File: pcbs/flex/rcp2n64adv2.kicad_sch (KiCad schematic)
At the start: 17 parts, among them J1 Conn_01x01, J2 Conn_01x01, J3 Conn_01x01, J3.1 Conn_01x01, J4 Conn_01x01, J5 Conn_01x01, J6 Conn_01x30, U1 74LVC1G17, X1 n64_rcp_vid_aud_out_no_3v3_con, X2 Conn_01x01

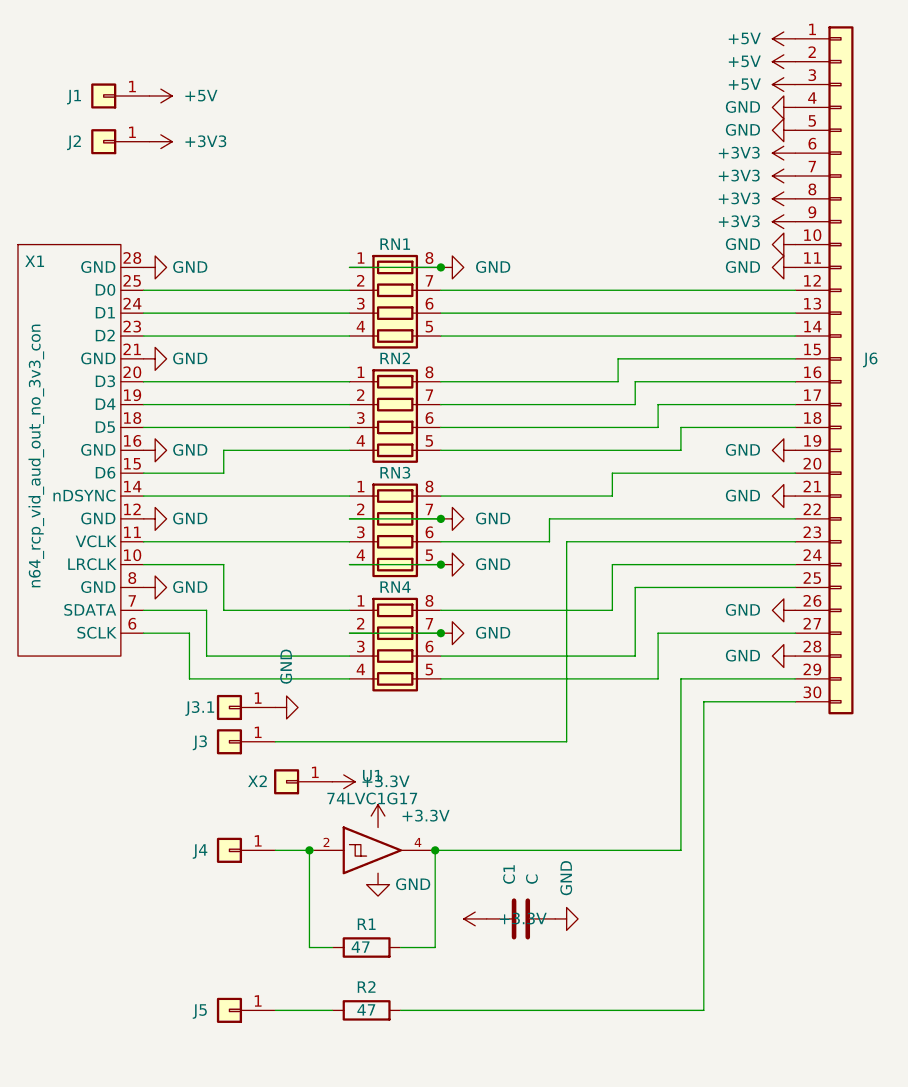
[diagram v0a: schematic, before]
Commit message: update flex PCB with minor changes, e.g. added a logo
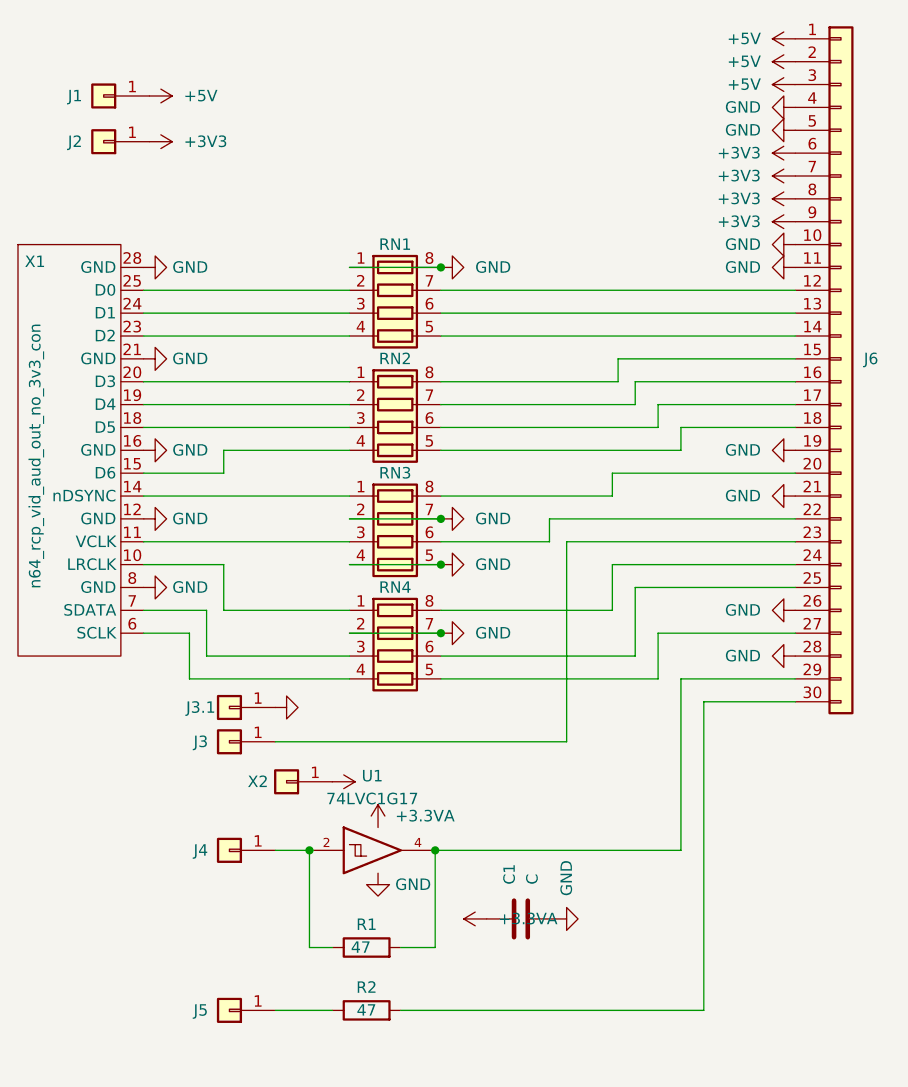
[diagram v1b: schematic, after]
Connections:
- net +3V3: no longer C1.1, U1.5 (VCC), X2.1 (Pin_1)
- new net +3.3VA: C1.1, U1.5 (VCC), X2.1 (Pin_1)
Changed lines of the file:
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@@
       (effects (font (size 1.27 1.27)) hide)
     )
-    (property "Value" "GND" (id 1) (at 74.9299 126.365 0)
+    (property "Value" "" (id 1) (at 74.9299 126.365 0)
       (effects (font (size 1.27 1.27)) (justify left))
     )
@@
     (pin "1")
   )
+  (symbol (lib_id "power:+3.3VA") (at 97.155 152.4 90) (unit 1)
+    (in_bom yes) (on_board yes) (fields_autoplaced)
+    (property "Reference" "#PWR?" (id 0) (at 100.965 152.4 0)
+      (effects (font (size 1.27 1.27)) hide)
+    )
+    (property "Value" "+3.3VA" (id 1) (at 98.425 152.3999 90)
+      (effects (font (size 1.27 1.27)) (justify right))
+    )
+    (property "Footprint" "" (id 2) (at 97.155 152.4 0)
+      (effects (font (size 1.27 1.27)) hide)
+    )
+    (property "Datasheet" "" (id 3) (at 97.155 152.4 0)
+      (effects (font (size 1.27 1.27)) hide)
+    )
+    (pin "1")
+  )
   (symbol (lib_id "Connector_Generic:Conn_01x01") (at 68.58 162.56 180) (unit 1)
     (in_bom no) (on_board yes)
@@
     )
     (property "Datasheet" "" (id 3) (at 59.055 115.57 0)
+      (effects (font (size 1.27 1.27)) hide)
+    )
+    (pin "1")
+  )
+  (symbol (lib_id "power:+3.3VA") (at 80.01 137.16 270) (unit 1)
+    (in_bom yes) (on_board yes) (fields_autoplaced)
+    (property "Reference" "#PWR?" (id 0) (at 76.2 137.16 0)
+      (effects (font (size 1.27 1.27)) hide)
+    )
+    (property "Value" "" (id 1) (at 83.82 137.1599 90)
+      (effects (font (size 1.27 1.27)) (justify left))
+    )
+    (property "Footprint" "" (id 2) (at 80.01 137.16 0)
+      (effects (font (size 1.27 1.27)) hide)
+    )
+    (property "Datasheet" "" (id 3) (at 80.01 137.16 0)
       (effects (font (size 1.27 1.27)) hide)
     )
@@
     (pin "1")
   )
-  (symbol (lib_id "power:+3.3V") (at 85.09 142.24 0) (unit 1)
-    (in_bom yes) (on_board yes) (fields_autoplaced)
-    (property "Reference" "#PWR0131" (id 0) (at 85.09 146.05 0)
-      (effects (font (size 1.27 1.27)) hide)
-    )
-    (property "Value" "+3.3V" (id 1) (at 87.63 140.9699 0)
-      (effects (font (size 1.27 1.27)) (justify left))
-    )
-    (property "Footprint" "" (id 2) (at 85.09 142.24 0)
-      (effects (font (size 1.27 1.27)) hide)
-    )
-    (property "Datasheet" "" (id 3) (at 85.09 142.24 0)
-      (effects (font (size 1.27 1.27)) hide)
-    )
-    (pin "1")
-  )
   (symbol (lib_id "power:GND") (at 92.075 120.65 90) (unit 1)
     (in_bom yes) (on_board yes) (fields_autoplaced)
@@
     (pin "1")
   )
-  (symbol (lib_id "power:+3.3V") (at 97.155 152.4 90) (unit 1)
-    (in_bom yes) (on_board yes) (fields_autoplaced)
-    (property "Reference" "#PWR0132" (id 0) (at 100.965 152.4 0)
-      (effects (font (size 1.27 1.27)) hide)
-    )
-    (property "Value" "+3.3V" (id 1) (at 98.425 152.3999 90)
-      (effects (font (size 1.27 1.27)) (justify right))
-    )
-    (property "Footprint" "" (id 2) (at 97.155 152.4 0)
-      (effects (font (size 1.27 1.27)) hide)
-    )
-    (property "Datasheet" "" (id 3) (at 97.155 152.4 0)
-      (effects (font (size 1.27 1.27)) hide)
-    )
-    (pin "1")
-  )
   (symbol (lib_id "power:GND") (at 92.075 113.03 90) (unit 1)
     (in_bom yes) (on_board yes) (fields_autoplaced)
@@
     (pin "1")
   )
-  (symbol (lib_id "power:+3.3V") (at 80.01 137.16 270) (unit 1)
-    (in_bom yes) (on_board yes) (fields_autoplaced)
-    (property "Reference" "#PWR0128" (id 0) (at 76.2 137.16 0)
-      (effects (font (size 1.27 1.27)) hide)
-    )
-    (property "Value" "+3.3V" (id 1) (at 83.185 137.1599 90)
-      (effects (font (size 1.27 1.27)) (justify left))
-    )
-    (property "Footprint" "" (id 2) (at 80.01 137.16 0)
-      (effects (font (size 1.27 1.27)) hide)
-    )
-    (property "Datasheet" "" (id 3) (at 80.01 137.16 0)
+  (symbol (lib_id "power:+3.3VA") (at 85.09 142.24 0) (unit 1)
+    (in_bom yes) (on_board yes) (fields_autoplaced)
+    (property "Reference" "#PWR?" (id 0) (at 85.09 146.05 0)
+      (effects (font (size 1.27 1.27)) hide)
+    )
+    (property "Value" "+3.3VA" (id 1) (at 86.995 140.9699 0)
+      (effects (font (size 1.27 1.27)) (justify left))
+    )
+    (property "Footprint" "" (id 2) (at 85.09 142.24 0)
+      (effects (font (size 1.27 1.27)) hide)
+    )
+    (property "Datasheet" "" (id 3) (at 85.09 142.24 0)
       (effects (font (size 1.27 1.27)) hide)
     )
@@
       (reference "#PWR0127") (unit 1) (value "GND") (footprint "")
     )
-    (path "/ebb00ccd-2cad-4af3-a4f4-9438755cb2c5"
-      (reference "#PWR0128") (unit 1) (value "+3.3V") (footprint "")
-    )
     (path "/b2464271-55c9-4c32-af2d-a4274a0cfecc"
       (reference "#PWR0129") (unit 1) (value "GND") (footprint "")
@@
       (reference "#PWR0130") (unit 1) (value "GND") (footprint "")
     )
-    (path "/d570e93c-5545-48d4-af35-1e19dc141390"
-      (reference "#PWR0131") (unit 1) (value "+3.3V") (footprint "")
-    )
-    (path "/e26c6331-4e64-4c88-af8e-b4f5a8b35c72"
-      (reference "#PWR0132") (unit 1) (value "+3.3V") (footprint "")
+    (path "/a2c5c77a-ce8a-4ada-ae7a-3089f5e18dfa"
+      (reference "#PWR?") (unit 1) (value "+3.3VA") (footprint "")
+    )
+    (path "/b68922d3-d7bc-4a97-8a9b-74840f074a00"
+      (reference "#PWR?") (unit 1) (value "+3.3VA") (footprint "")
+    )
+    (path "/e9ff7066-aa8f-4937-aa8c-dac2c54d75e7"
+      (reference "#PWR?") (unit 1) (value "+3.3VA") (footprint "")
     )
     (path "/fe28d019-2901-415f-bbfb-9066de361fb0"

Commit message: update main PCB with minor changes, e.g. ensure that solder mask bridges between 0.5mm pitched pads has min. 0.1mm thickness
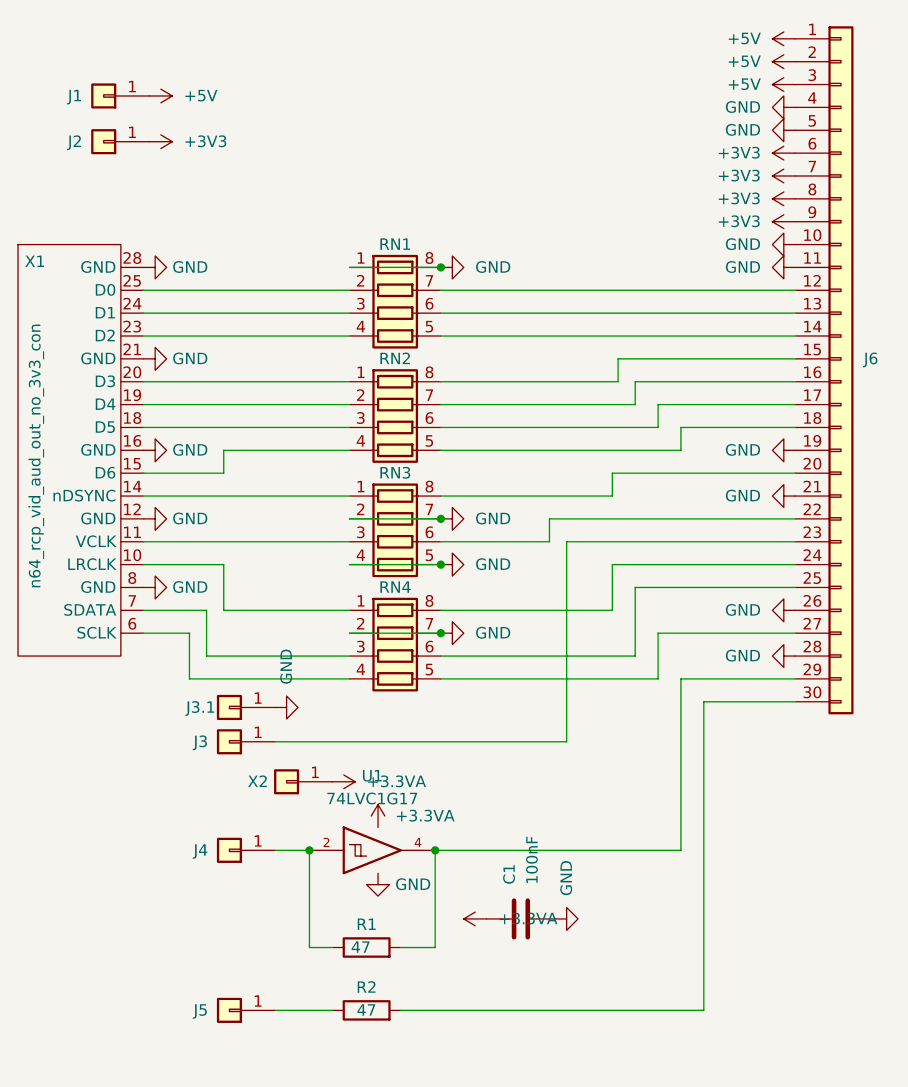
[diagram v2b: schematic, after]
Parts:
- C1: value C -> 100nF
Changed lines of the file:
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@@
       (effects (font (size 1.27 1.27)) hide)
     )
-    (property "Value" "" (id 1) (at 74.9299 126.365 0)
+    (property "Value" "GND" (id 1) (at 74.9299 126.365 0)
       (effects (font (size 1.27 1.27)) (justify left))
     )
@@
       (effects (font (size 1.27 1.27)) hide)
     )
-    (property "Value" "" (id 1) (at 83.82 137.1599 90)
+    (property "Value" "+3.3VA" (id 1) (at 83.82 137.1599 90)
       (effects (font (size 1.27 1.27)) (justify left))
     )
@@
       (effects (font (size 1.27 1.27)) (justify left))
     )
-    (property "Value" "C" (id 1) (at 102.2349 148.59 0)
+    (property "Value" "100nF" (id 1) (at 102.2349 148.59 0)
       (effects (font (size 1.27 1.27)) (justify left))
     )
@@
     )
     (path "/fe28d019-2901-415f-bbfb-9066de361fb0"
-      (reference "C1") (unit 1) (value "C") (footprint "Capacitor_SMD:C_0603_1608Metric_Pad1.08x0.95mm_HandSolder")
+      (reference "C1") (unit 1) (value "100nF") (footprint "Capacitor_SMD:C_0603_1608Metric_Pad1.08x0.95mm_HandSolder")
     )
     (path "/67679f6e-1f3a-4f43-8e31-3367e2bcf78f"

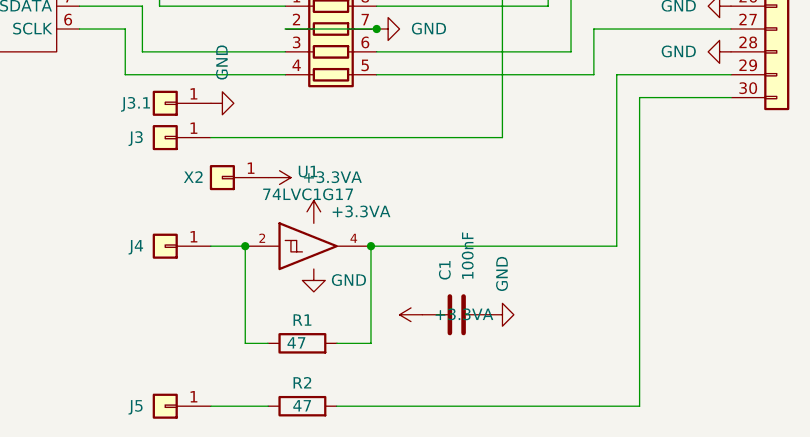
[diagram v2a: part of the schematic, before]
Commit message: update flex PCB: - add a feedback path for VI-Deblur - optimize implementation around U1 - add logo and license text to silkscreen
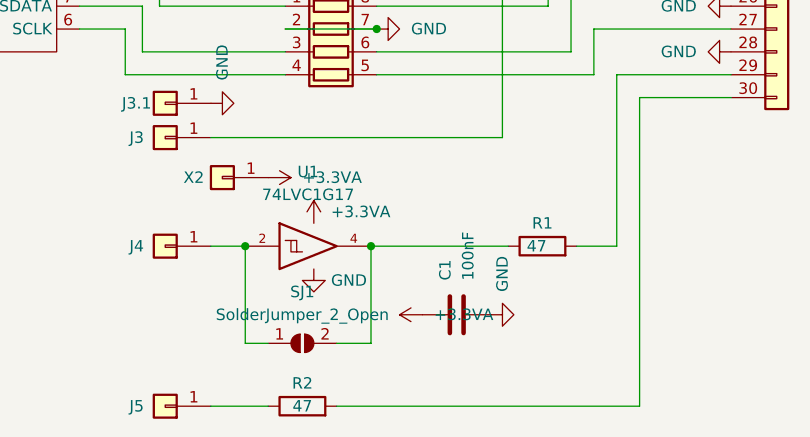
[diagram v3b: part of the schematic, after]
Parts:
- added SJ1: SolderJumper_2_Open, Jumper:SolderJumper-2_P1.3mm_Open_RoundedPad1.0x1.5mm, symbol Jumper:SolderJumper_2_Open
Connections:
- net at J4.1 (Pin_1), U1.2: now also SJ1.1 (A); no longer R1.1
- net at J6.29 (Pin_29), R1.2: no longer U1.4
- new net: R1.1, SJ1.2 (B), U1.4
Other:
- company: (none) -> Peter 'borti4938' Bartmann
- title: (none) -> RCP2N64Adv2
- moved on the sheet: R1
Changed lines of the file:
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@@
 (kicad_sch (version 20211123) (generator eeschema)
   (paper "A4")
+  (title_block
+    (title "RCP2N64Adv2")
+    (rev "v20220903")
+    (company "Peter 'borti4938' Bartmann")
+    (comment 1 "Schematic and PCB (c) 2021, 2022 by Peter Bartmann")
+    (comment 2 "Licensed under CERN-OHL-W v2")
+  )
   (junction (at 77.47 144.78) (diameter 0) (color 0 0 0 0)
   )
@@
     (stroke (width 0) (type default) (color 0 0 0 0))
   )
+  (wire (pts (xy 106.68 144.78) (xy 91.44 144.78))
+    (stroke (width 0) (type default) (color 0 0 0 0))
+  )
   (wire (pts (xy 116.205 95.25) (xy 131.445 95.25))
     (stroke (width 0) (type default) (color 0 0 0 0))
@@
     (stroke (width 0) (type default) (color 0 0 0 0))
   )
-  (wire (pts (xy 118.745 144.78) (xy 91.44 144.78))
+  (wire (pts (xy 118.745 144.78) (xy 114.3 144.78))
     (stroke (width 0) (type default) (color 0 0 0 0))
   )
@@
     (pin "1")
   )
-  (symbol (lib_id "Device:R") (at 83.82 155.575 90) (unit 1)
+  (symbol (lib_id "Device:R") (at 110.49 144.78 90) (unit 1)
     (in_bom no) (on_board yes)
-    (property "Reference" "R1" (id 0) (at 83.82 153.035 90))
-    (property "Value" "47" (id 1) (at 83.185 155.575 90))
-    (property "Footprint" "Resistor_SMD:R_0603_1608Metric_Pad0.98x0.95mm_HandSolder" (id 2) (at 83.82 157.353 90)
-      (effects (font (size 1.27 1.27)) hide)
-    )
-    (property "Datasheet" "~" (id 3) (at 83.82 155.575 0)
+    (property "Reference" "R1" (id 0) (at 110.49 142.24 90))
+    (property "Value" "47" (id 1) (at 109.855 144.78 90))
+    (property "Footprint" "Resistor_SMD:R_0603_1608Metric_Pad0.98x0.95mm_HandSolder" (id 2) (at 110.49 146.558 90)
+      (effects (font (size 1.27 1.27)) hide)
+    )
+    (property "Datasheet" "~" (id 3) (at 110.49 144.78 0)
       (effects (font (size 1.27 1.27)) hide)
     )
@@
     (pin "1")
   )
+  (symbol (lib_id "Jumper:SolderJumper_2_Open") (at 83.82 155.575 0) (unit 1)
+    (in_bom no) (on_board yes) (fields_autoplaced)
+    (property "Reference" "SJ1" (id 0) (at 83.82 149.86 0))
+    (property "Value" "SolderJumper_2_Open" (id 1) (at 83.82 152.4 0))
+    (property "Footprint" "Jumper:SolderJumper-2_P1.3mm_Open_RoundedPad1.0x1.5mm" (id 2) (at 83.82 155.575 0)
+      (effects (font (size 1.27 1.27)) hide)
+    )
+    (property "Datasheet" "~" (id 3) (at 83.82 155.575 0)
+      (effects (font (size 1.27 1.27)) hide)
+    )
+    (pin "1")
+    (pin "2")
+  )
   (symbol (lib_id "power:+3.3VA") (at 97.155 152.4 90) (unit 1)
     (in_bom yes) (on_board yes) (fields_autoplaced)
-    (property "Reference" "#PWR?" (id 0) (at 100.965 152.4 0)
+    (property "Reference" "#PWR0132" (id 0) (at 100.965 152.4 0)
       (effects (font (size 1.27 1.27)) hide)
     )
@@
   (symbol (lib_id "power:+3.3VA") (at 80.01 137.16 270) (unit 1)
     (in_bom yes) (on_board yes) (fields_autoplaced)
-    (property "Reference" "#PWR?" (id 0) (at 76.2 137.16 0)
+    (property "Reference" "#PWR0128" (id 0) (at 76.2 137.16 0)
       (effects (font (size 1.27 1.27)) hide)
     )
@@
   (symbol (lib_id "power:+3.3VA") (at 85.09 142.24 0) (unit 1)
     (in_bom yes) (on_board yes) (fields_autoplaced)
-    (property "Reference" "#PWR?" (id 0) (at 85.09 146.05 0)
+    (property "Reference" "#PWR0131" (id 0) (at 85.09 146.05 0)
       (effects (font (size 1.27 1.27)) hide)
     )
@@
       (reference "#PWR0127") (unit 1) (value "GND") (footprint "")
     )
+    (path "/b68922d3-d7bc-4a97-8a9b-74840f074a00"
+      (reference "#PWR0128") (unit 1) (value "+3.3VA") (footprint "")
+    )
     (path "/b2464271-55c9-4c32-af2d-a4274a0cfecc"
       (reference "#PWR0129") (unit 1) (value "GND") (footprint "")
@@
       (reference "#PWR0130") (unit 1) (value "GND") (footprint "")
     )
+    (path "/e9ff7066-aa8f-4937-aa8c-dac2c54d75e7"
+      (reference "#PWR0131") (unit 1) (value "+3.3VA") (footprint "")
+    )
     (path "/a2c5c77a-ce8a-4ada-ae7a-3089f5e18dfa"
-      (reference "#PWR?") (unit 1) (value "+3.3VA") (footprint "")
-    )
-    (path "/b68922d3-d7bc-4a97-8a9b-74840f074a00"
-      (reference "#PWR?") (unit 1) (value "+3.3VA") (footprint "")
-    )
-    (path "/e9ff7066-aa8f-4937-aa8c-dac2c54d75e7"
-      (reference "#PWR?") (unit 1) (value "+3.3VA") (footprint "")
+      (reference "#PWR0132") (unit 1) (value "+3.3VA") (footprint "")
     )
     (path "/fe28d019-2901-415f-bbfb-9066de361fb0"
@@
       (reference "RN4") (unit 1) (value "R_Pack04") (footprint "Resistor_SMD:R_Array_Convex_4x0603")
     )
+    (path "/8fb41a33-8fc0-4a8d-8ae7-94e234723f48"
+      (reference "SJ1") (unit 1) (value "SolderJumper_2_Open") (footprint "Jumper:SolderJumper-2_P1.3mm_Open_RoundedPad1.0x1.5mm")
+    )
     (path "/42e45e2c-9977-480b-a863-c6494dbed837"

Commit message: some BOM updates
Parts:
- R1: now in the parts list
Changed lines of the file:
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@@
   )
   (symbol (lib_id "Device:R") (at 110.49 144.78 90) (unit 1)
-    (in_bom no) (on_board yes)
+    (in_bom yes) (on_board yes)
     (property "Reference" "R1" (id 0) (at 110.49 142.24 90))
     (property "Value" "47" (id 1) (at 109.855 144.78 90))
